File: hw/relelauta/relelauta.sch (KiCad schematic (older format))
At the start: 51 parts, among them J1 serial_in, J2 serial_out, J3 arduino_5V, J4 coil_power, K1 RY5W-K, K2 RY5W-K, K3 RY5W-K, K4 RY5W-K, K5 RY5W-K, K6 RY5W-K, K7 RY5W-K, K8 RY5W-K, Q1 2N3904, Q2 2N3904, Q3 2N3904, Q4 2N3904, Q5 2N3904, Q6 2N3904, Q7 2N3904, Q8 2N3904, U1 74HC595

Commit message: Add test points and useful connectors
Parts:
- added J5: coil_power_out, Connectors_Terminal_Blocks:TerminalBlock_bornier-2_P5.08mm, symbol Connector:Conn_01x02_Male
- added J6: 5V_out, Pin_Headers:Pin_Header_Straight_1x02_Pitch2.54mm, symbol Connector:Conn_01x02_Male
- added TP1: data_in, Measurement_Points:Test_Point_Keystone_5019_Minature, symbol Connector:TestPoint
- added TP2: clock, Measurement_Points:Test_Point_Keystone_5019_Minature, symbol Connector:TestPoint
- added TP3: latch, Measurement_Points:Test_Point_Keystone_5019_Minature, symbol Connector:TestPoint
- added TP4: data_out, Measurement_Points:Test_Point_Keystone_5019_Minature, symbol Connector:TestPoint
- C1, C2: footprint (none) -> Capacitors_SMD:C_0805_HandSoldering
- D10, D9: footprint (none) -> LEDs:LED_0805_HandSoldering
- J1, J2: footprint (none) -> Pin_Headers:Pin_Header_Straight_1x03_Pitch2.54mm
- J3: footprint (none) -> Pin_Headers:Pin_Header_Straight_1x02_Pitch2.54mm
- J4: value coil_power -> coil_power_in; footprint (none) -> Connectors_Terminal_Blocks:TerminalBlock_bornier-2_P5.08mm
- R10, R9: footprint (none) -> Resistors_SMD:R_0805_HandSoldering
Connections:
- net +5V: now also J6.1 (Pin_1)
- net GND: now also J5.2 (Pin_2), J6.2 (Pin_2)
- net V_coil: now also J5.1 (Pin_1)
- net clock: now also TP2.1
- net data_in: now also TP1.1
- net data_out: now also TP4.1
- net latch: now also TP3.1
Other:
- moved on the sheet: J1
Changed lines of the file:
@@
 F 0 "C2" V 3100 4600 50  0000 C CNN
 F 1 "100n" V 3100 4450 50  0000 C CNN
-F 2 "" H 3200 4600 50  0001 C CNN
+F 2 "Capacitors_SMD:C_0805_HandSoldering" H 3200 4600 50  0001 C CNN
 F 3 "~" H 3200 4600 50  0001 C CNN
 	1    3200 4600
@@
 L Connector:Conn_01x03_Female J1
 U 1 1 5D02EB6D
-P 1550 5350
-F 0 "J1" H 1442 5635 50  0000 C CNN
-F 1 "serial_in" H 1442 5544 50  0000 C CNN
-F 2 "" H 1550 5350 50  0001 C CNN
-F 3 "~" H 1550 5350 50  0001 C CNN
-	1    1550 5350
+P 1300 5350
+F 0 "J1" H 1192 5635 50  0000 C CNN
+F 1 "serial_in" H 1192 5544 50  0000 C CNN
+F 2 "Pin_Headers:Pin_Header_Straight_1x03_Pitch2.54mm" H 1300 5350 50  0001 C CNN
+F 3 "~" H 1300 5350 50  0001 C CNN
+	1    1300 5350
 	-1   0    0    -1
 $EndComp
@@
 F 0 "J2" H 5072 5374 50  0000 R CNN
 F 1 "serial_out" H 5072 5283 50  0000 R CNN
-F 2 "" H 5100 5350 50  0001 C CNN
+F 2 "Pin_Headers:Pin_Header_Straight_1x03_Pitch2.54mm" H 5100 5350 50  0001 C CNN
 F 3 "~" H 5100 5350 50  0001 C CNN
 	1    5100 5350
@@
 F 0 "C1" H 2550 5600 50  0000 C CNN
 F 1 "100n" H 2900 5600 50  0000 C CNN
-F 2 "" H 2700 5600 50  0001 C CNN
+F 2 "Capacitors_SMD:C_0805_HandSoldering" H 2700 5600 50  0001 C CNN
 F 3 "~" H 2700 5600 50  0001 C CNN
 	1    2700 5600
 	-1   0    0    1
 $EndComp
-Text GLabel 1750 5350 2    50   Input ~ 0
+Text GLabel 1950 5350 2    50   Input ~ 0
 clock
-Text GLabel 1750 5450 2    50   Input ~ 0
+Text GLabel 1950 5450 2    50   Input ~ 0
 latch
 Text GLabel 4900 5350 0    50   Input ~ 0
@@
 Text GLabel 3000 5100 0    50   Input ~ 0
 clock
-Text GLabel 1750 5250 2    50   Input ~ 0
+Text GLabel 1950 5250 2    50   Input ~ 0
 data_in
-Text GLabel 3800 5800 2    50   Input ~ 0
+Text GLabel 4000 5800 2    50   Input ~ 0
 data_out
 Text GLabel 4900 5250 0    50   Input ~ 0
@@
 F 0 "D9" V 1239 2533 50  0000 R CNN
 F 1 "ARDUINO" V 1148 2533 50  0000 R CNN
-F 2 "" H 1200 2650 50  0001 C CNN
+F 2 "LEDs:LED_0805_HandSoldering" H 1200 2650 50  0001 C CNN
 F 3 "~" H 1200 2650 50  0001 C CNN
 	1    1200 2650
@@
 F 0 "R9" H 1270 2996 50  0000 L CNN
 F 1 "10k" H 1270 2905 50  0000 L CNN
-F 2 "" V 1130 2950 50  0001 C CNN
+F 2 "Resistors_SMD:R_0805_HandSoldering" V 1130 2950 50  0001 C CNN
 F 3 "~" H 1200 2950 50  0001 C CNN
 	1    1200 2950
@@
 F 0 "J3" H 1258 4131 50  0000 C CNN
 F 1 "arduino_5V" H 1258 4040 50  0000 C CNN
-F 2 "" H 1150 3950 50  0001 C CNN
+F 2 "Pin_Headers:Pin_Header_Straight_1x02_Pitch2.54mm" H 1150 3950 50  0001 C CNN
 F 3 "~" H 1150 3950 50  0001 C CNN
 	1    1150 3950
@@
 P 1150 4400
 F 0 "J4" H 1258 4581 50  0000 C CNN
-F 1 "coil_power" H 1258 4490 50  0000 C CNN
-F 2 "" H 1150 4400 50  0001 C CNN
+F 1 "coil_power_in" H 1258 4490 50  0000 C CNN
+F 2 "Connectors_Terminal_Blocks:TerminalBlock_bornier-2_P5.08mm" H 1150 4400 50  0001 C CNN
 F 3 "~" H 1150 4400 50  0001 C CNN
 	1    1150 4400
@@
 F 0 "D10" V 1989 2532 50  0000 R CNN
 F 1 "COIL" V 1898 2532 50  0000 R CNN
-F 2 "" H 1950 2650 50  0001 C CNN
+F 2 "LEDs:LED_0805_HandSoldering" H 1950 2650 50  0001 C CNN
 F 3 "~" H 1950 2650 50  0001 C CNN
 	1    1950 2650
@@
 F 0 "R10" H 2020 2996 50  0000 L CNN
 F 1 "10k" H 2020 2905 50  0000 L CNN
-F 2 "" V 1880 2950 50  0001 C CNN
+F 2 "Resistors_SMD:R_0805_HandSoldering" V 1880 2950 50  0001 C CNN
 F 3 "~" H 1950 2950 50  0001 C CNN
 	1    1950 2950
@@
 Wire Notes Line
 	3100 3850 3100 600
+$Comp
+L Connector:Conn_01x02_Male J6
+U 1 1 5D1830F7
+P 1900 3950
+F 0 "J6" H 2008 4131 50  0000 C CNN
+F 1 "5V_out" H 2008 4040 50  0000 C CNN
+F 2 "Pin_Headers:Pin_Header_Straight_1x02_Pitch2.54mm" H 1900 3950 50  0001 C CNN
+F 3 "~" H 1900 3950 50  0001 C CNN
+	1    1900 3950
+	1    0    0    -1
+$EndComp
+$Comp
+L power:+5V #PWR040
+U 1 1 5D1830FD
+P 2100 3950
+F 0 "#PWR040" H 2100 3800 50  0001 C CNN
+F 1 "+5V" V 2115 4078 50  0000 L CNN
+F 2 "" H 2100 3950 50  0001 C CNN
+F 3 "" H 2100 3950 50  0001 C CNN
+	1    2100 3950
+	0    1    1    0
+$EndComp
+$Comp
+L power:GND #PWR041
+U 1 1 5D183103
+P 2100 4050
+F 0 "#PWR041" H 2100 3800 50  0001 C CNN
+F 1 "GND" V 2105 3922 50  0000 R CNN
+F 2 "" H 2100 4050 50  0001 C CNN
+F 3 "" H 2100 4050 50  0001 C CNN
+	1    2100 4050
+	0    -1   -1   0
+$EndComp
+$Comp
+L Connector:Conn_01x02_Male J5
+U 1 1 5D189A4E
+P 1850 4350
+F 0 "J5" H 1958 4531 50  0000 C CNN
+F 1 "coil_power_out" H 1958 4440 50  0000 C CNN
+F 2 "Connectors_Terminal_Blocks:TerminalBlock_bornier-2_P5.08mm" H 1850 4350 50  0001 C CNN
+F 3 "~" H 1850 4350 50  0001 C CNN
+	1    1850 4350
+	1    0    0    -1
+$EndComp
+Text GLabel 2050 4350 2    50   Input ~ 0
+V_coil
+$Comp
+L power:GND #PWR039
+U 1 1 5D189A55
+P 2050 4450
+F 0 "#PWR039" H 2050 4200 50  0001 C CNN
+F 1 "GND" V 2055 4322 50  0000 R CNN
+F 2 "" H 2050 4450 50  0001 C CNN
+F 3 "" H 2050 4450 50  0001 C CNN
+	1    2050 4450
+	0    -1   -1   0
+$EndComp
+$Comp
+L Connector:TestPoint TP1
+U 1 1 5D190C6D
+P 1550 5600
+F 0 "TP1" H 1600 5850 50  0000 R CNN
+F 1 "data_in" V 1550 6200 50  0000 R CNN
+F 2 "Measurement_Points:Test_Point_Keystone_5019_Minature" H 1750 5600 50  0001 C CNN
+F 3 "~" H 1750 5600 50  0001 C CNN
+	1    1550 5600
+	-1   0    0    1
+$EndComp
+$Comp
+L Connector:TestPoint TP2
+U 1 1 5D19BF09
+P 1700 5600
+F 0 "TP2" H 1750 5850 50  0000 R CNN
+F 1 "clock" V 1700 6100 50  0000 R CNN
+F 2 "Measurement_Points:Test_Point_Keystone_5019_Minature" H 1900 5600 50  0001 C CNN
+F 3 "~" H 1900 5600 50  0001 C CNN
+	1    1700 5600
+	-1   0    0    1
+$EndComp
+$Comp
+L Connector:TestPoint TP3
+U 1 1 5D1A1C01
+P 1850 5600
+F 0 "TP3" H 1900 5850 50  0000 R CNN
+F 1 "latch" V 1850 6100 50  0000 R CNN
+F 2 "Measurement_Points:Test_Point_Keystone_5019_Minature" H 2050 5600 50  0001 C CNN
+F 3 "~" H 2050 5600 50  0001 C CNN
+	1    1850 5600
+	-1   0    0    1
+$EndComp
+Wire Wire Line
+	1500 5250 1550 5250
+Wire Wire Line
+	1950 5350 1700 5350
+Wire Wire Line
+	1700 5350 1700 5600
+Wire Wire Line
+	1950 5450 1850 5450
+Wire Wire Line
+	1850 5450 1850 5600
+Wire Wire Line
+	1550 5600 1550 5250
+Connection ~ 1550 5250
+Wire Wire Line
+	1550 5250 1950 5250
+Wire Wire Line
+	1500 5350 1700 5350
+Connection ~ 1700 5350
+Wire Wire Line
+	1500 5450 1850 5450
+Connection ~ 1850 5450
+Wire Wire Line
+	4000 5800 3900 5800
+Wire Wire Line
+	3900 5800 3900 5900
+Connection ~ 3900 5800
+Wire Wire Line
+	3900 5800 3800 5800
+$Comp
+L Connector:TestPoint TP4
+U 1 1 5D1E3E27
+P 3900 5900
+F 0 "TP4" H 3950 6150 50  0000 R CNN
+F 1 "data_out" H 4050 6250 50  0000 R CNN
+F 2 "Measurement_Points:Test_Point_Keystone_5019_Minature" H 4100 5900 50  0001 C CNN
+F 3 "~" H 4100 5900 50  0001 C CNN
+	1    3900 5900
+	-1   0    0    1
+$EndComp
 $EndSCHEMATC

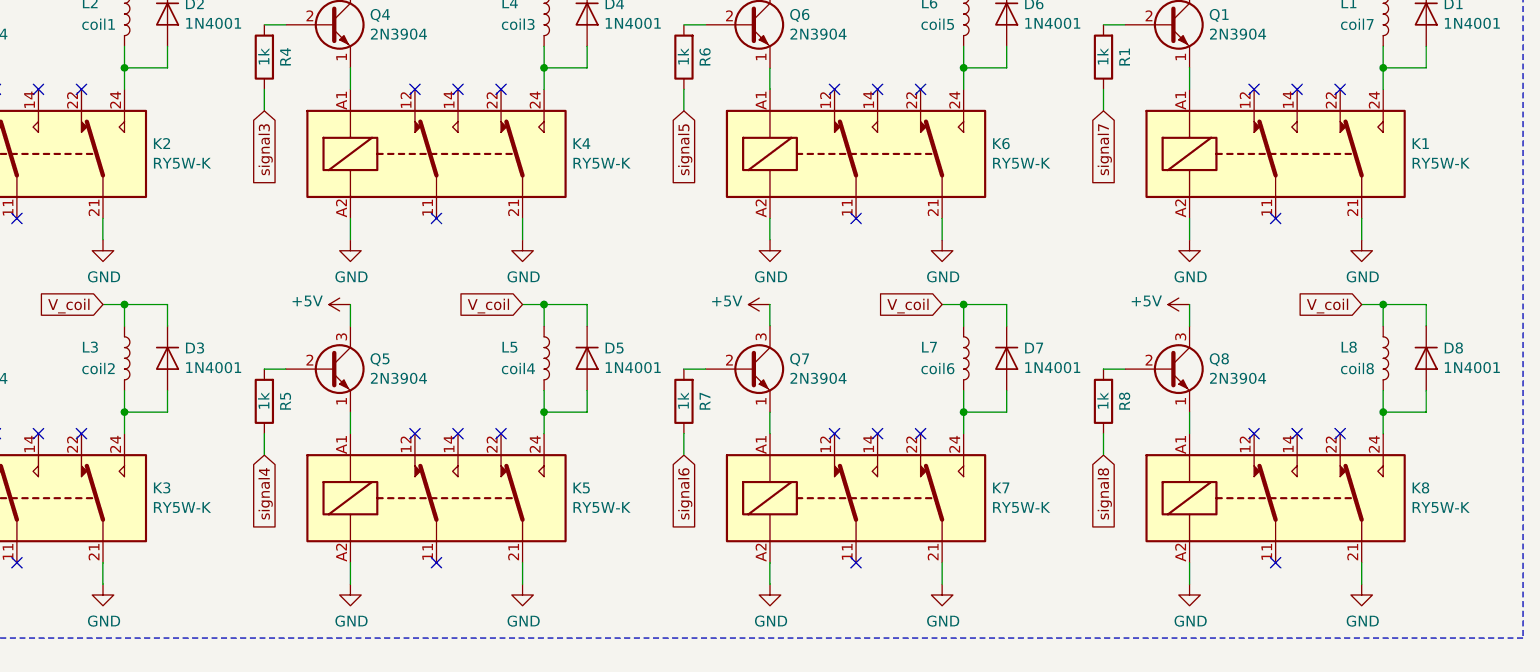
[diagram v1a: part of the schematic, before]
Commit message: Completed PCB layout
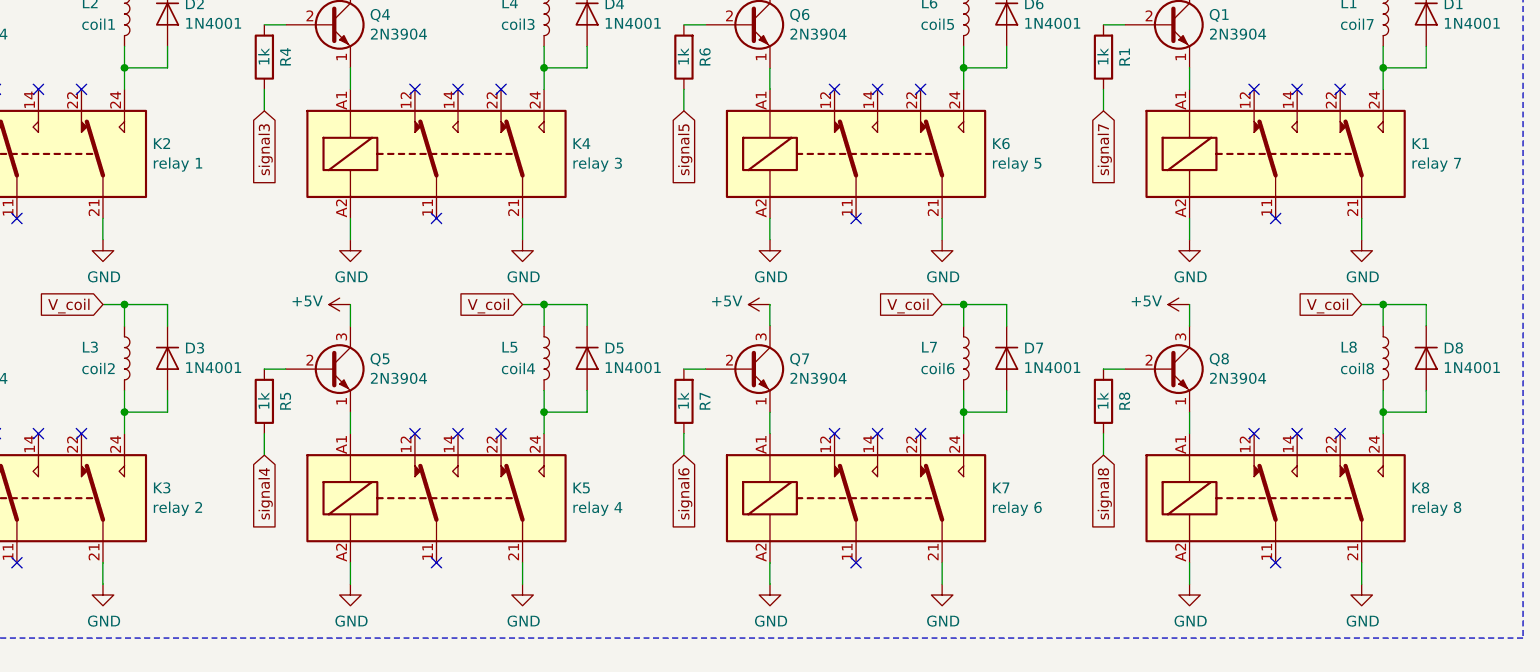
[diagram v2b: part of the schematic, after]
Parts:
- D1: footprint Connectors_Terminal_Blocks:TerminalBlock_bornier-2_P5.08mm -> Diodes_THT:D_DO-41_SOD81_P7.62mm_Horizontal
- K1: value RY5W-K -> relay 7
- K2: value RY5W-K -> relay 1
- K3: value RY5W-K -> relay 2
- K4: value RY5W-K -> relay 3
- K5: value RY5W-K -> relay 4
- K6: value RY5W-K -> relay 5
- K7: value RY5W-K -> relay 6
- K8: value RY5W-K -> relay 8
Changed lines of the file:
@@
 P 9950 1600
 F 0 "K1" H 10580 1646 50  0000 L CNN
-F 1 "RY5W-K" H 10580 1555 50  0000 L CNN
+F 1 "relay 7" H 10580 1555 50  0000 L CNN
 F 2 "RELE2:RY5W-K" H 11300 1570 50  0001 C CNN
 F 3 "http://www.relpol.pl/en/content/download/13766/168095/file/e_RM84.pdf" H 9750 1600 50  0001 C CNN
@@
 F 0 "D1" V 10604 1029 50  0000 L CNN
 F 1 "1N4001" V 10695 1029 50  0000 L CNN
-F 2 "Connectors_Terminal_Blocks:TerminalBlock_bornier-2_P5.08mm" H 10650 950 50  0001 C CNN
+F 2 "Diodes_THT:D_DO-41_SOD81_P7.62mm_Horizontal" H 10650 950 50  0001 C CNN
 F 3 "~" H 10650 950 50  0001 C CNN
 	1    10650 950
@@
 P 9950 3200
 F 0 "K8" H 10580 3246 50  0000 L CNN
-F 1 "RY5W-K" H 10580 3155 50  0000 L CNN
+F 1 "relay 8" H 10580 3155 50  0000 L CNN
 F 2 "RELE2:RY5W-K" H 11300 3170 50  0001 C CNN
 F 3 "http://www.relpol.pl/en/content/download/13766/168095/file/e_RM84.pdf" H 9750 3200 50  0001 C CNN
@@
 P 8000 1600
 F 0 "K6" H 8630 1646 50  0000 L CNN
-F 1 "RY5W-K" H 8630 1555 50  0000 L CNN
+F 1 "relay 5" H 8630 1555 50  0000 L CNN
 F 2 "RELE2:RY5W-K" H 9350 1570 50  0001 C CNN
 F 3 "http://www.relpol.pl/en/content/download/13766/168095/file/e_RM84.pdf" H 7800 1600 50  0001 C CNN
@@
 P 8000 3200
 F 0 "K7" H 8630 3246 50  0000 L CNN
-F 1 "RY5W-K" H 8630 3155 50  0000 L CNN
+F 1 "relay 6" H 8630 3155 50  0000 L CNN
 F 2 "RELE2:RY5W-K" H 9350 3170 50  0001 C CNN
 F 3 "http://www.relpol.pl/en/content/download/13766/168095/file/e_RM84.pdf" H 7800 3200 50  0001 C CNN
@@
 P 6050 1600
 F 0 "K4" H 6680 1646 50  0000 L CNN
-F 1 "RY5W-K" H 6680 1555 50  0000 L CNN
+F 1 "relay 3" H 6680 1555 50  0000 L CNN
 F 2 "RELE2:RY5W-K" H 7400 1570 50  0001 C CNN
 F 3 "http://www.relpol.pl/en/content/download/13766/168095/file/e_RM84.pdf" H 5850 1600 50  0001 C CNN
@@
 P 6050 3200
 F 0 "K5" H 6680 3246 50  0000 L CNN
-F 1 "RY5W-K" H 6680 3155 50  0000 L CNN
+F 1 "relay 4" H 6680 3155 50  0000 L CNN
 F 2 "RELE2:RY5W-K" H 7400 3170 50  0001 C CNN
 F 3 "http://www.relpol.pl/en/content/download/13766/168095/file/e_RM84.pdf" H 5850 3200 50  0001 C CNN
@@
 P 4100 1600
 F 0 "K2" H 4730 1646 50  0000 L CNN
-F 1 "RY5W-K" H 4730 1555 50  0000 L CNN
+F 1 "relay 1" H 4730 1555 50  0000 L CNN
 F 2 "RELE2:RY5W-K" H 5450 1570 50  0001 C CNN
 F 3 "http://www.relpol.pl/en/content/download/13766/168095/file/e_RM84.pdf" H 3900 1600 50  0001 C CNN
@@
 P 4100 3200
 F 0 "K3" H 4730 3246 50  0000 L CNN
-F 1 "RY5W-K" H 4730 3155 50  0000 L CNN
+F 1 "relay 2" H 4730 3155 50  0000 L CNN
 F 2 "RELE2:RY5W-K" H 5450 3170 50  0001 C CNN
 F 3 "http://www.relpol.pl/en/content/download/13766/168095/file/e_RM84.pdf" H 3900 3200 50  0001 C CNN

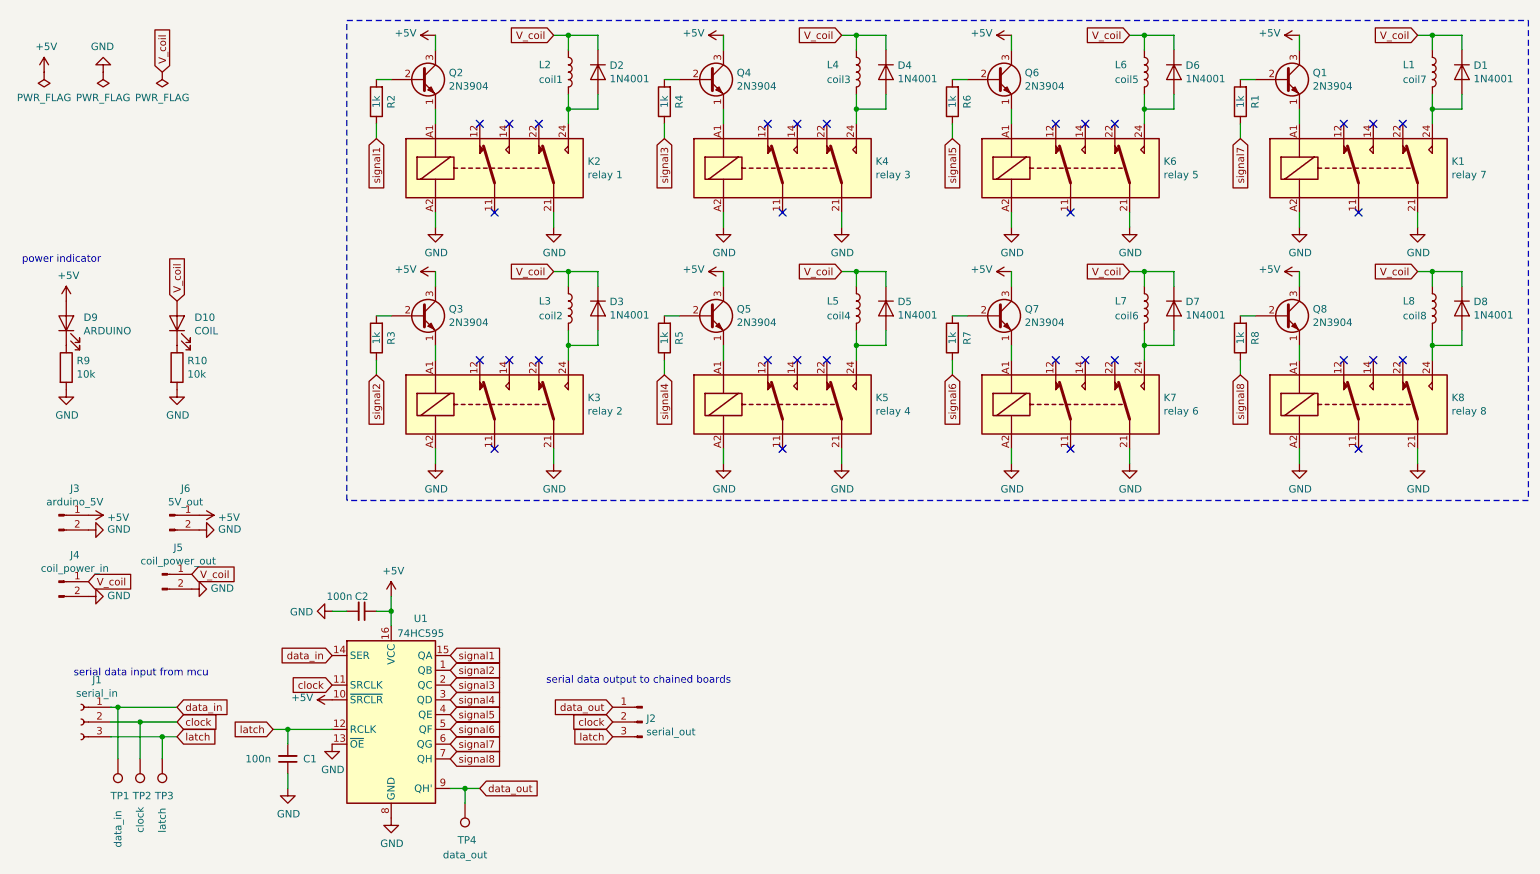
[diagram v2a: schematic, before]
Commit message: Fixed NPN transistors on the wrong side of load in the schematic by changing them to PNP transistors.
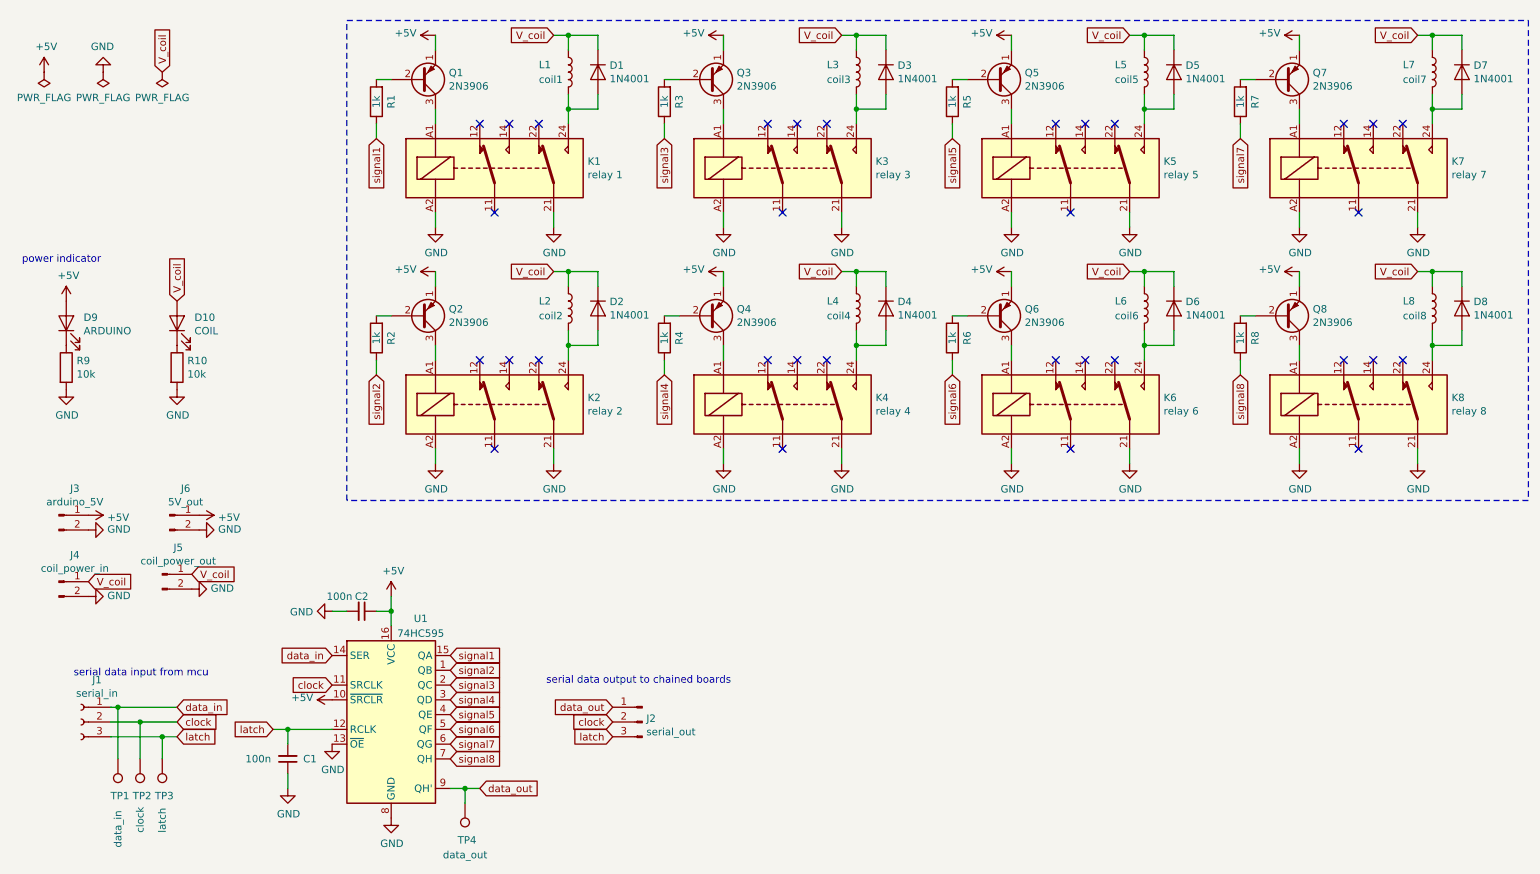
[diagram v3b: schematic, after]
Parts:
- removed Q1, Q2, Q3, Q4, Q5, Q6, Q7, Q8: 2N3904, TO_SOT_Packages_THT:TO-92_Inline_Narrow_Oval, symbol Transistor_BJT:2N3904
- added Q1, Q2, Q3, Q4, Q5, Q6, Q7, Q8: 2N3906, TO_SOT_Packages_THT:TO-92_Inline_Narrow_Oval, symbol Transistor_BJT:2N3906
- renumbered D2 to D1, D3 to D2, D4 to D3, D5 to D4, D6 to D5, D7 to D6, D1 to D7, K2 to K1, K3 to K2, K4 to K3, K5 to K4, K6 to K5, K7 to K6, K1 to K7, L2 to L1, L3 to L2, L4 to L3, L5 to L4, L6 to L5, L7 to L6, L1 to L7, R2 to R1, R3 to R2, R4 to R3, R5 to R4, R6 to R5, R7 to R6, R1 to R7
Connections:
- net +5V: now also Q1.1 (E), Q2.1 (E), Q3.1 (E), Q4.1 (E), Q5.1 (E), Q6.1 (E), Q7.1 (E), Q8.1 (E)
- net at K7.A1: now also Q7.3 (C)
- net at R7.2: now also Q7.2 (B)
- net at K8.A1: now also Q8.3 (C)
- net at R8.2: now also Q8.2 (B)
- net at K5.A1: now also Q5.3 (C)
- net at R5.2: now also Q5.2 (B)
- net at K6.A1: now also Q6.3 (C)
- net at R6.2: now also Q6.2 (B)
- net at K3.A1: now also Q3.3 (C)
- net at R3.2: now also Q3.2 (B)
- net at K4.A1: now also Q4.3 (C)
- net at R4.2: now also Q4.2 (B)
- net at K1.A1: now also Q1.3 (C)
- net at R1.2: now also Q1.2 (B)
- net at K2.A1: now also Q2.3 (C)
- net at R2.2: now also Q2.2 (B)
